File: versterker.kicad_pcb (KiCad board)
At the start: 2 copper layers, 50 x 50 mm, 45 parts, among them J1 J_Barreljack_3.5mm_Wurth_TH, J2 J_3.5mm_jack_SJ1-3523N, Q1 Q_IRFZ44NPBF_N-Channel_Infine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, Q2 Q_IRFZ44NPBF_N-Channel_Infine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, U1 U_LM317_TH, U2 U_LM317_TH, U4 U_LM393N_NOPB, U5 U_TC4427M_Microchip, U6 U_555_timer, U7 U_LM3914N-1_NOPB

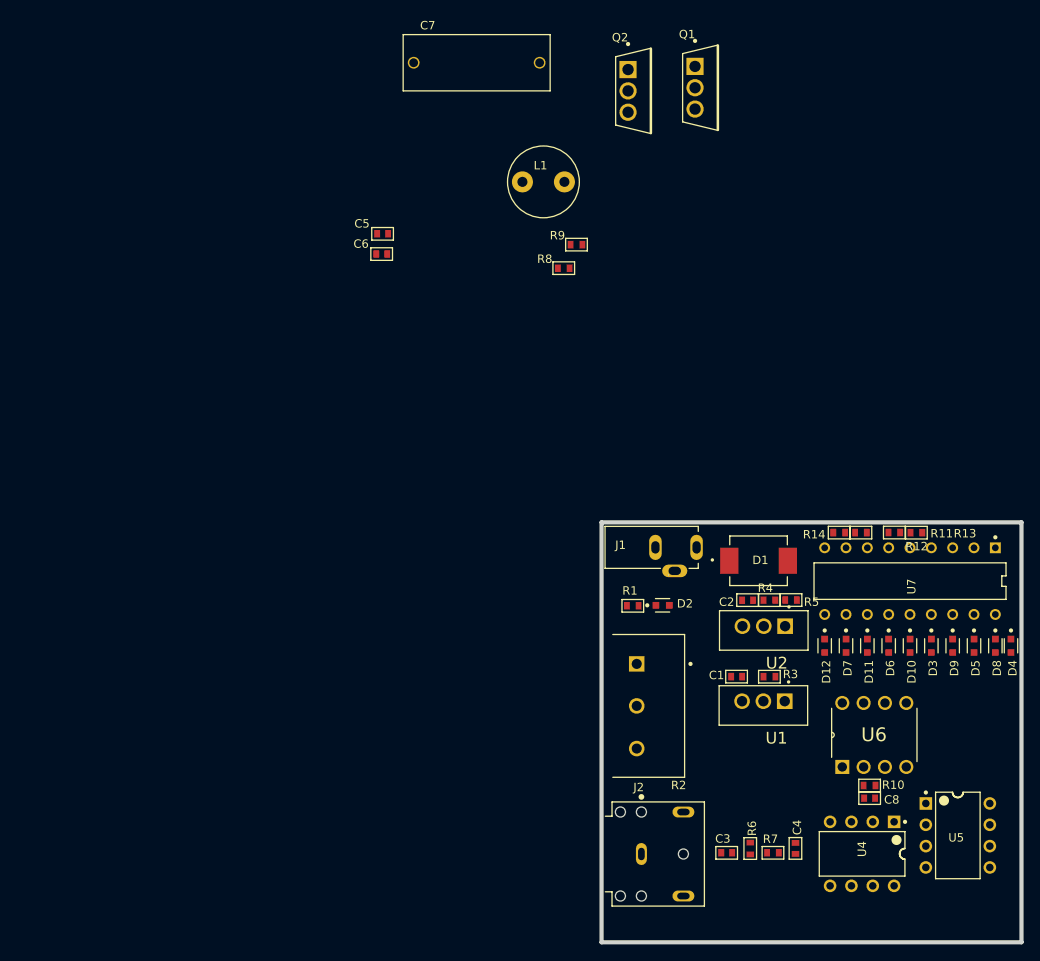
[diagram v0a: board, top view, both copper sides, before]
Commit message: added raspberry pi hat pcb outline and layout
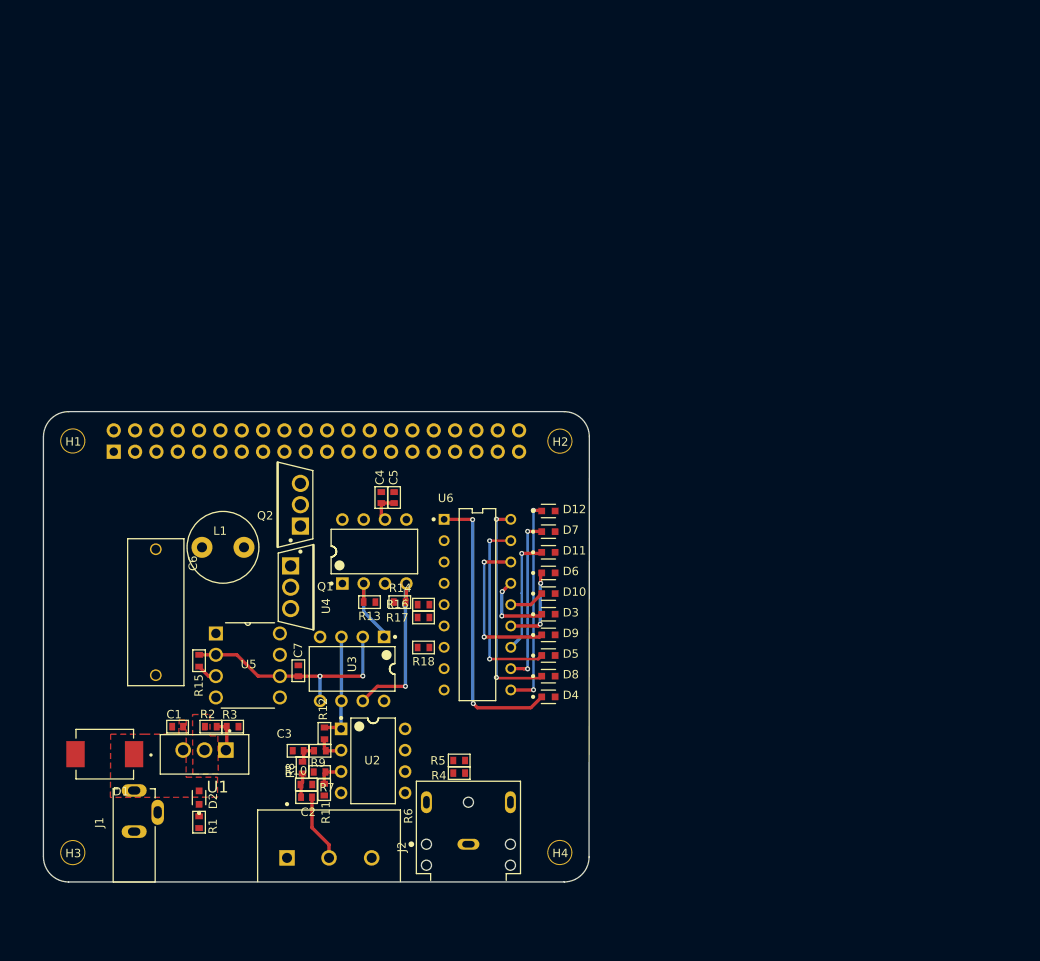
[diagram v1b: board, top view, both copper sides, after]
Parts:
- removed C8: C_1nF_0603_50V, MAIN_PCB_LIB:C_0603
- removed U7: U_LM3914N-1_NOPB, MAIN_PCB_LIB:U_LM3914_TI_DIP
- added H1: 3mm_Mounting_Hole, project_footprints:NPTH_3mm_ID, F.Cu at (82.0, 64.3)
- added H2: 3mm_Mounting_Hole, project_footprints:NPTH_3mm_ID, F.Cu at (140.0, 64.3)
- added H3: 3mm_Mounting_Hole, project_footprints:NPTH_3mm_ID, F.Cu at (82.0, 113.3)
- added H4: 3mm_Mounting_Hole, project_footprints:NPTH_3mm_ID, F.Cu at (140.0, 113.3)
- added J3: 40HAT, Connector_PinSocket_2.54mm:PinSocket_2x20_P2.54mm_Vertical, B.Cu at (86.9, 65.6)
- added R15: R_2K_0603, MAIN_PCB_LIB:R_0603, F.Cu at (97.1, 90.5)
- added R16: R_4K7_0603, MAIN_PCB_LIB:R_0603, F.Cu at (123.8, 83.8)
- added R17: R_1K_0603, MAIN_PCB_LIB:R_0603, F.Cu at (123.8, 85.3)
- added R18: R_3K16_0603, MAIN_PCB_LIB:R_0603, F.Cu at (123.8, 88.9)
- added U3: U_LM393N_NOPB, MAIN_PCB_LIB:U_TI_LM393N_NOPB, F.Cu at (115.3, 91.5)
- C2: value C_100nF_0603_50V -> C_1.5uF_0603_25V
- C3: value C_1.5uF_0603_25V -> C_390pF_0603_50V
- C4: value C_390pF_0603_50V -> C_4.7uF_0603_25V
- C5: value C_4.7uF_0603_25V -> C_100nF_0603_50V
- C6: value C_100nF_0603_50V -> C_680nF_TH_450V; footprint MAIN_PCB_LIB:C_0603 -> MAIN_PCB_LIB:C_ECWFD_Panasonic
- C7: value C_680nF_TH_450V -> C_1nF_0603_50V; footprint MAIN_PCB_LIB:C_ECWFD_Panasonic -> MAIN_PCB_LIB:C_0603
- R10: value R_2K_0603 -> R_10K_0603
- R11: value R_4K7_0603 -> R_1K5_0603
- R12: value R_1K_0603 -> R_60.4K_0603
- R13: value R_3K4_0603 -> R_10K_0603
- R14: value R_3K16_0603 -> R_10K_0603
- R2: value R_10K_Potmeter -> R_3K_0603; footprint MAIN_PCB_LIB:R_TH_POT_P160series -> MAIN_PCB_LIB:R_0603
- R3: value R_3K_0603 -> R_9K1_0603
- R4: value R_3K_0603 -> R_10K_0603
- R5: value R_9K1_0603 -> R_10K_0603
- R6: value R_10K_0603 -> R_10K_Potmeter; footprint MAIN_PCB_LIB:R_0603 -> MAIN_PCB_LIB:R_TH_POT_P160series
- R8: value R_100K_0603 -> R_10K_0603
- R9: value R_100K_0603 -> R_20K_0603
- U2: value U_LM317_TH -> U_LM358AP_TI_DIP; footprint MAIN_PCB_LIB:U_LM317_TI_TH -> MAIN_PCB_LIB:U_LM358AP_TI_DIP
- U4: value U_LM393N_NOPB -> U_TC4427M_Microchip; footprint MAIN_PCB_LIB:U_TI_LM393N_NOPB -> MAIN_PCB_LIB:U_8_DIP_TC4427CPA_Microchip
- U5: value U_TC4427M_Microchip -> U_555_timer; footprint MAIN_PCB_LIB:U_8_DIP_TC4427CPA_Microchip -> MAIN_PCB_LIB:U_LM555CN
- U6: value U_555_timer -> U_LM3914N-1_NOPB; footprint MAIN_PCB_LIB:U_LM555CN -> MAIN_PCB_LIB:U_LM3914_TI_DIP
- moved U5 82.4 mm to (106.7, 94.8)
- moved D1 81.2 mm to (85.8, 101.6), turned to 180 degrees
- moved Q1 76.5 mm to (108.6, 81.7)
- moved C7 75.4 mm to (108.9, 91.7), turned to 270 degrees
- moved R11 74.5 mm to (112.0, 105.8), turned to 90 degrees
- moved R12 74.4 mm to (112.0, 99.1), turned to 90 degrees
- moved J1 68.8 mm to (89.3, 116.8), turned to 90 degrees
- moved U4 68.3 mm to (118.0, 77.5), turned to 90 degrees
- moved R9 67.6 mm to (111.5, 101.2)
- moved R8 67.1 mm to (109.4, 103.2), turned to 90 degrees
- moved C1 66.8 mm to (94.5, 98.3)
- moved U1 66.8 mm to (97.7, 101.6)
- moved R10 65.5 mm to (111.4, 103.7), turned to 0 degrees
- moved C4 64.6 mm to (118.8, 71.0)
- moved R3 64.2 mm to (101.1, 98.3)
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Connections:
- C2 pad 1: /9V -> Net-(C2-Pad1)
- C2 pad 2: GND -> Net-(C2-Pad2)
- C3 pad 2: /Amplifier/L_channel -> GND
- C5 pad 1: Net-(C5-Pad1) -> Net-(C4-Pad1)
- C6 pad 1: Net-(C5-Pad1) -> /Amplifier/Amplifier_output
- C7 pad 1: /Amplifier/Amplifier_output -> /Triangle_wave
- J2 pad 3: /Amplifier/L_channel -> /Amplifier/R_channel
- Q1 pad 2: /High_power -> /Amplifier/9V
- R10 pad 1: /Triangle_wave -> Net-(R10-Pad1)
- R11 pad 1: Net-(R11-Pad1) -> Net-(R10-Pad1)
- R11 pad 2: /High_power -> GND
- R12 pad 1: Net-(R11-Pad1) -> Net-(R12-Pad1)
- R12 pad 2: GND -> Net-(R12-Pad2)
- R13 pad 1: GND -> Net-(R13-Pad1)
- R14 pad 2: Net-(R13-Pad2) -> Net-(R14-Pad2)
- R2 pad 1: Net-(R2-Pad1) -> /5V
- R2 pad 2: GND -> Net-(R2-Pad2)
- R3 pad 1: /High_power -> Net-(R2-Pad2)
- R3 pad 2: Net-(R2-Pad1) -> GND
- R4 pad 1: /5V -> /Amplifier/R_channel
- R5 pad 2: GND -> /Amplifier/L_channel
- R6 pad 1: Net-(C3-Pad1) -> Net-(R4-Pad2)
- R6 pad 2: GND -> Net-(C2-Pad2)
- R7 pad 1: Net-(C4-Pad1) -> Net-(C2-Pad1)
- R7 pad 2: Net-(C3-Pad1) -> GND
- R8 pad 1: Net-(Q1-Pad1) -> Net-(C3-Pad1)
- R8 pad 2: GND -> Net-(C2-Pad1)
- R9 pad 1: Net-(Q2-Pad1) -> Net-(R12-Pad2)
- R9 pad 2: GND -> Net-(C3-Pad1)
- U1 pad 1: Net-(R2-Pad1) -> Net-(R2-Pad2)
- U1 pad 2: /High_power -> /5V
- U2 pad 1: Net-(R4-Pad2) -> Net-(R12-Pad1)
- U2 pad 2: /5V -> Net-(R12-Pad2)
- U2 pad 3: /9V -> Net-(R10-Pad1)
- U4 pad 2: /Triangle_wave -> Net-(R13-Pad2)
- U4 pad 3: Net-(C4-Pad1) -> GND
- U4 pad 4: GND -> Net-(R14-Pad2)
- U4 pad 5: /Triangle_wave -> Net-(Q2-Pad1)
- U4 pad 7: Net-(U4-Pad7) -> Net-(Q1-Pad1)
- U4 pad 8: /5V -> Net-(U4-Pad8)
- U5 pad 1: Net-(U5-Pad1) -> GND
- U5 pad 2: Net-(U4-Pad1) -> /Triangle_wave
- U5 pad 3: GND -> Net-(R15-Pad2)
- U5 pad 4: Net-(U4-Pad7) -> /5V
- U5 pad 5: Net-(Q2-Pad1) -> Net-(U5-Pad5)
- U5 pad 6: Net-(C5-Pad1) -> /Triangle_wave
- U5 pad 7: Net-(Q1-Pad1) -> Net-(U5-Pad7)
- U5 pad 8: Net-(U5-Pad8) -> /5V
- U6 pad 1: GND -> Net-(D4-Pad1)
- U6 pad 2: /Triangle_wave -> GND
- U6 pad 3: Net-(R10-Pad2) -> /9V
- U6 pad 4: /5V -> GND
- U6 pad 6: /Triangle_wave -> Net-(R18-Pad1)
- U6 pad 7: Net-(U6-Pad7) -> Net-(R18-Pad1)
- U6 pad 8: /5V -> GND
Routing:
- net Net-(D4-Pad1): track 0.00 -> 34.2 mm, vias 0 -> 2
- net /Triangle_wave: track 0.00 -> 28.2 mm, vias 0 -> 2
- net Net-(D8-Pad1): track 0.00 -> 26.0 mm, vias 0 -> 2
- net Net-(D12-Pad1): track 0.00 -> 25.2 mm, vias 0 -> 2
- net Net-(D5-Pad1): track 0.00 -> 23.0 mm, vias 0 -> 2
- net Net-(R14-Pad2): track 0.00 -> 20.3 mm, vias 0 -> 1
- net Net-(D7-Pad1): track 0.00 -> 20.2 mm, vias 0 -> 2
- net Net-(D9-Pad1): track 0.00 -> 19.2 mm, vias 0 -> 2
- net Net-(D11-Pad1): track 0.00 -> 14.2 mm, vias 0 -> 1
- net Net-(R12-Pad1): track 0.00 -> 13.1 mm
- net Net-(D6-Pad1): track 0.00 -> 9.77 mm, vias 0 -> 2
- net Net-(R13-Pad2): track 0.00 -> 9.58 mm
- net Net-(D3-Pad1): track 0.00 -> 9.19 mm, vias 0 -> 2
- net Net-(C2-Pad2): track 0.00 -> 8.06 mm
- net Net-(D10-Pad1): track 0.00 -> 4.23 mm
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- added copper zone on F.Cu, net /5V
- added copper zone on F.Cu, net /9V
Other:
- board size 50 x 50 mm -> 65 x 56 mm
- net class Default: trace_width 0.25 -> 0.15; via_dia 0.8 -> 0.6; via_drill 0.4 -> 0.3
- rule pad_to_mask_clearance: 0 -> 0.1
- rule trace_min: 0.2 -> 0.1
- rule via_min_drill: 0.3 -> 0.2
- rule via_min_size: 0.4 -> 0.5

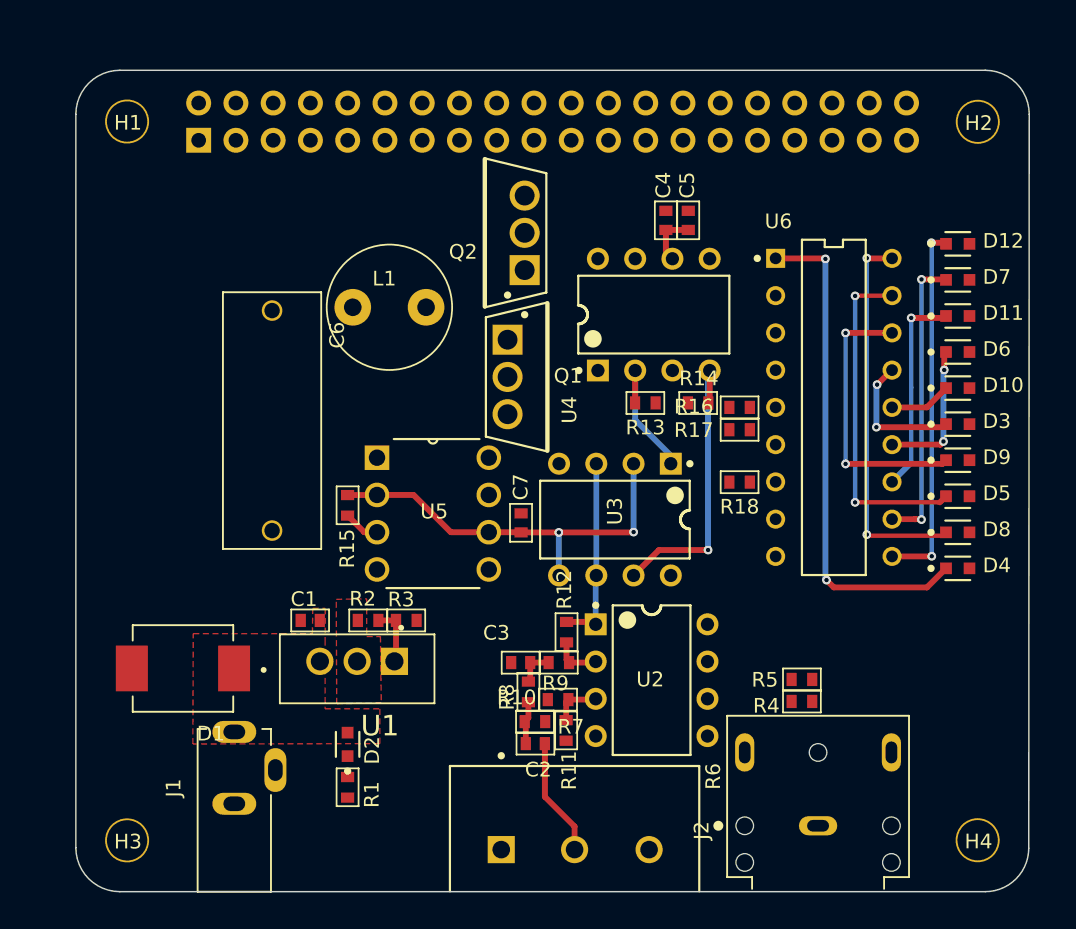
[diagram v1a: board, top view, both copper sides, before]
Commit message: changed everything to 9V and changed inductor to match one in stock
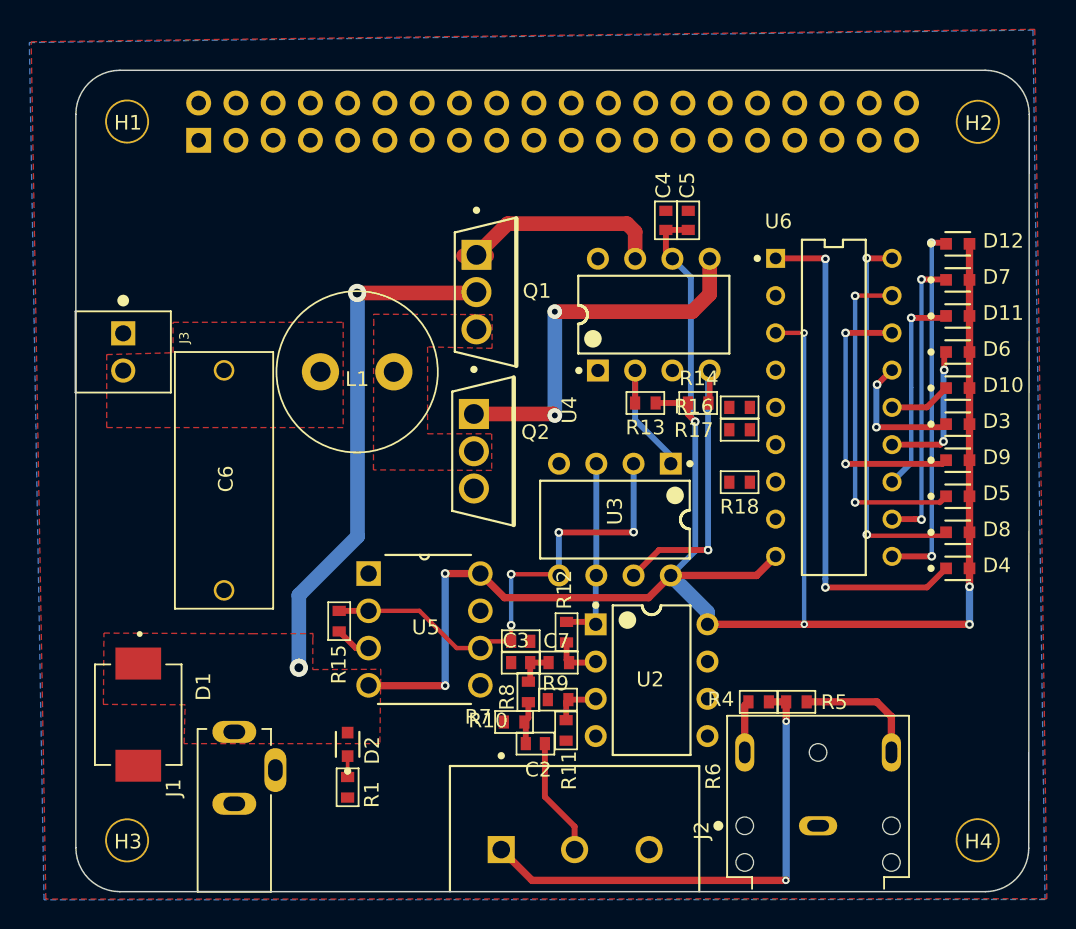
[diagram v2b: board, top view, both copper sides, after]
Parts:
- removed C1: C_100nF_0603_50V, MAIN_PCB_LIB:C_0603
- removed R2: R_3K_0603, MAIN_PCB_LIB:R_0603
- removed R3: R_9K1_0603, MAIN_PCB_LIB:R_0603
- removed U1: U_LM317_TH, MAIN_PCB_LIB:U_LM317_TI_TH
- added J3: J_2_screwterminal_2.54_282834-2, MAIN_PCB_LIB:J_2_screwterminal_2.54, F.Cu at (81.8, 80.0)
- L1: value L_22uH_8095_WU-TI -> L_22uH_RFS1113_coilcraft_TH; footprint MAIN_PCB_LIB:L_WE-TI_8095Series -> MAIN_PCB_LIB:L_RFS1113_coilcraft
- moved Q2 15.1 mm to (106.3, 86.8), turned to 0 degrees
- moved C7 8.08 mm to (108.9, 99.8), turned to 180 degrees
- moved R15 7.92 mm to (96.5, 98.4)
- moved U5 7.92 mm to (106.1, 102.8)
- moved Q1 6.16 mm to (106.5, 75.9)
- moved C6 5.23 mm to (88.7, 88.8)
- moved L1 4.92 mm to (97.7, 81.4)
- moved D1 4.38 mm to (82.8, 104.8), turned to 270 degrees
- moved R4 2.95 mm to (125.1, 103.9), turned to 180 degrees
- moved R5 1.57 mm to (127.7, 103.9)
- moved R7 1.43 mm to (108.4, 105.2), turned to 0 degrees
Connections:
- net /Amplifier/Amplifier_output renamed Net-(C6-Pad1)
- C4 pad 1: Net-(C4-Pad1) -> /9V
- C5 pad 1: Net-(C4-Pad1) -> /9V
- Q1 pad 2: /Amplifier/9V -> /9V
- R13 pad 1: Net-(R13-Pad1) -> /9V
- R14 pad 1: Net-(R14-Pad1) -> /9V
- U2 pad 8: /Amplifier/9V -> /9V
- U3 pad 8: /5V -> /9V
- U4 pad 6: Net-(C4-Pad1) -> /9V
- U5 pad 4: /5V -> /9V
- U5 pad 8: /5V -> /9V
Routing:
- net /9V: track 0.01 -> 172.9 mm, vias 0 -> 9
- net Net-(R4-Pad2): track 0.00 -> 33.7 mm, vias 0 -> 2
- net Net-(Q2-Pad1): track 0.00 -> 26.1 mm, vias 0 -> 2
- net Net-(Q1-Pad1): track 0.00 -> 15.4 mm
- net /Amplifier/L_channel: track 0.00 -> 8.64 mm
- net /Triangle_wave: track 28.2 -> 33.6 mm, vias 2 -> 4
- net Net-(R2-Pad2): track 4.04 -> 0.00 mm
- net Net-(C4-Pad1): track 3.67 -> 0.00 mm
- net /Amplifier/R_channel: track 0.00 -> 3.55 mm
- net Net-(D2-Pad1): track 0.00 -> 1.42 mm
- added copper zone on B.Cu, net GND
- added copper zone on F.Cu, net GND
- added copper zone on F.Cu, net Net-(C6-Pad1)
- added copper zone on F.Cu, net Net-(L1-Pad1)
- removed copper zone on F.Cu, net /5V
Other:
- net class Default: trace_width 0.15 -> 0.2
- net class default 2 added: clearance 0.2, trace_width 0.3, via_dia 0.5, via_drill 0.3
- rule trace_min: 0.1 -> 0.2

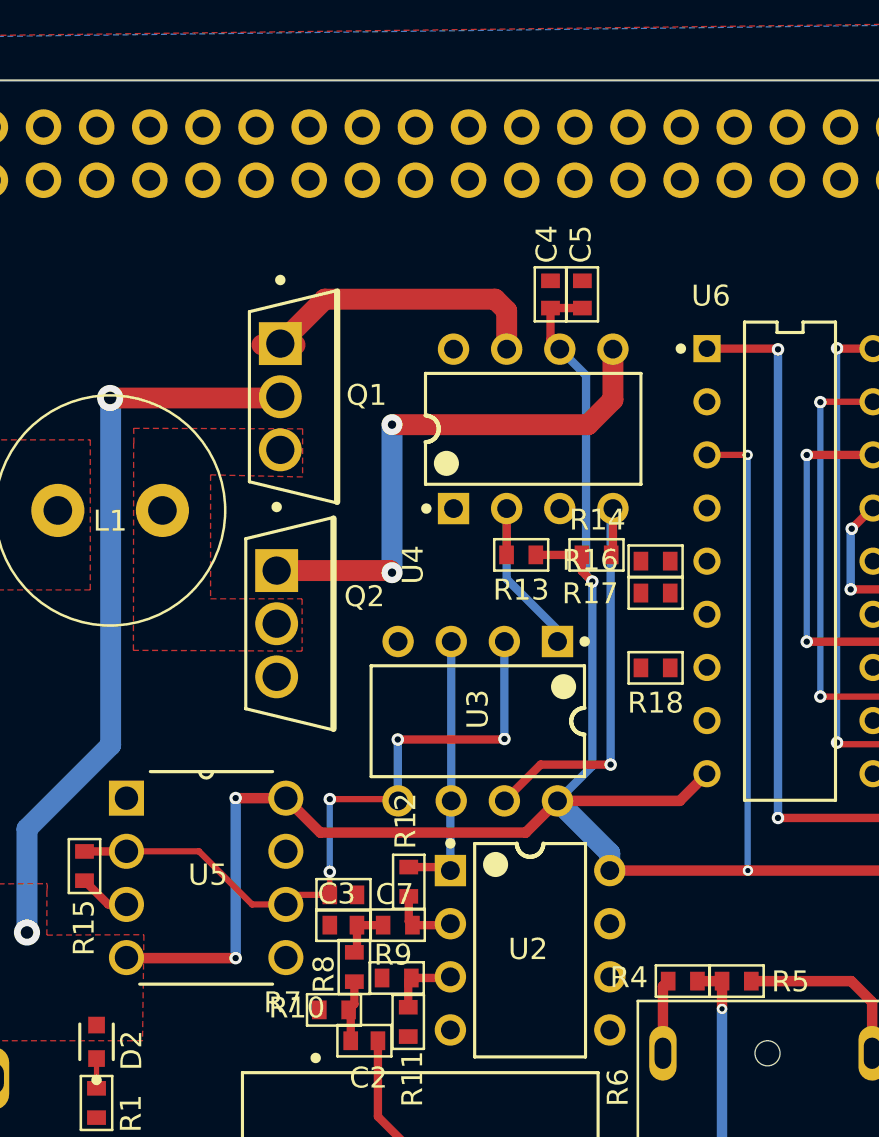
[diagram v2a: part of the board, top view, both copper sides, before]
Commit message: changed vu meter circuit
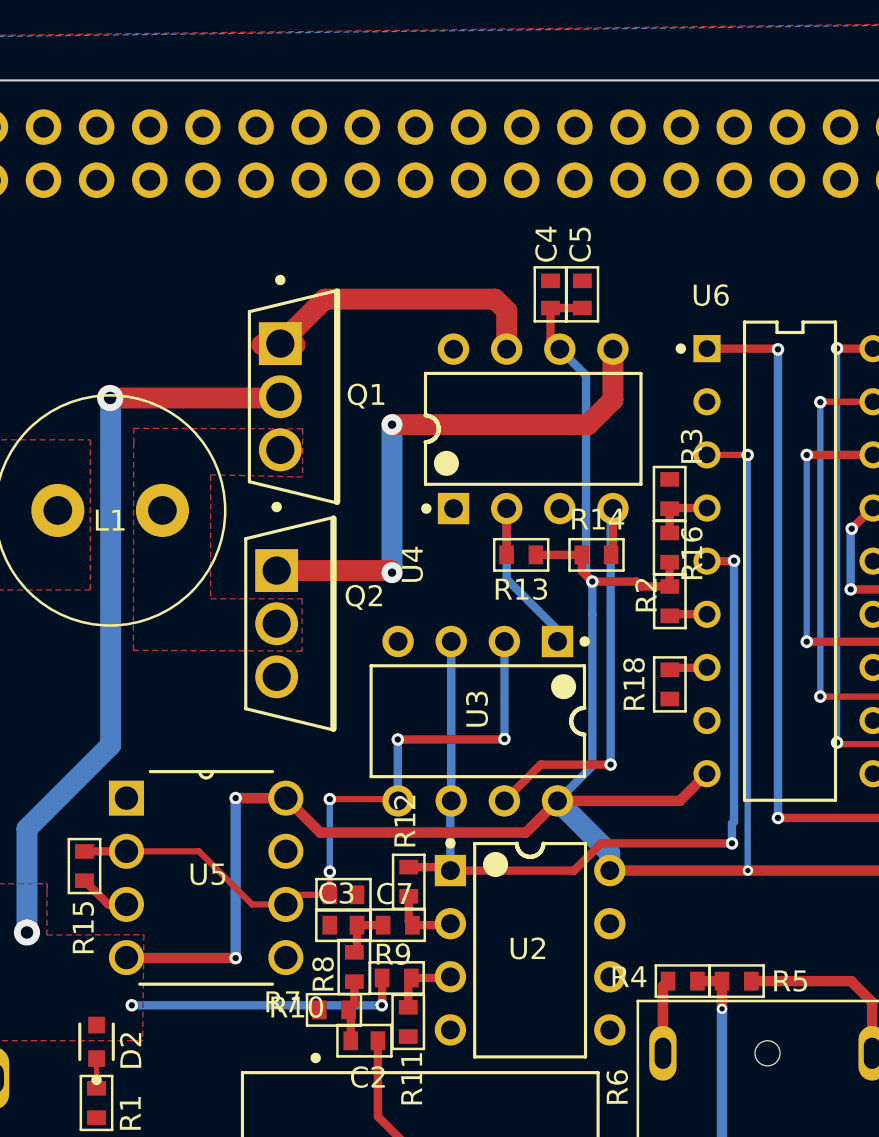
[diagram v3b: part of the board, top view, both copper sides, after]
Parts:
- removed R17: R_1K_0603, MAIN_PCB_LIB:R_0603
- added R2: R_10K_0603, MAIN_PCB_LIB:R_0603, F.Cu at (124.5, 83.2)
- added R3: R_2K_0603, MAIN_PCB_LIB:R_0603, F.Cu at (124.5, 80.6)
- R16: value R_4K7_0603 -> R_25K5_0603
- U2: value U_LM358AP_TI_DIP -> Val**
- moved R16 2.03 mm to (124.5, 85.7), turned to 270 degrees
- moved R18 1.04 mm to (124.5, 89.7), turned to 270 degrees
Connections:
- R10 pad 2: Net-(R10-Pad2) -> /9V
- R12 pad 1: Net-(R12-Pad1) -> /ampsignal
- R16 pad 2: /High_power -> /9V
- R18 pad 1: Net-(R18-Pad1) -> GND
- R18 pad 2: GND -> Net-(R18-Pad2)
- U2 pad 1: Net-(R12-Pad1) -> /ampsignal
- U3 pad 3: Net-(R12-Pad1) -> /ampsignal
- U3 pad 6: Net-(R12-Pad1) -> /ampsignal
- U6 pad 4: GND -> Net-(R2-Pad1)
- U6 pad 5: Net-(R16-Pad1) -> /ampsignal
- U6 pad 6: Net-(R18-Pad1) -> Net-(R16-Pad1)
- U6 pad 7: Net-(R18-Pad1) -> Net-(R18-Pad2)
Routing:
- net /ampsignal: track 0.00 -> 41.9 mm, vias 0 -> 2
- net /9V: track 172.9 -> 191.1 mm, vias 9 -> 11
- net Net-(R12-Pad1): track 13.1 -> 0.00 mm
- net Net-(R2-Pad1): track 0.00 -> 2.96 mm
- net Net-(R18-Pad2): track 0.00 -> 1.77 mm
- net Net-(R16-Pad1): track 0.00 -> 1.71 mm
